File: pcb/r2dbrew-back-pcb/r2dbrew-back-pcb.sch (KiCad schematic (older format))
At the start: 38 parts, among them IC1 74HC238, IC2 TLC5971, IC3 FT230X, IC4 LM1117, IC5 ATMEGA328P, J1 USB, J2 PSI1, J3 PSI2, J4 RGB1, J5 RGB2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

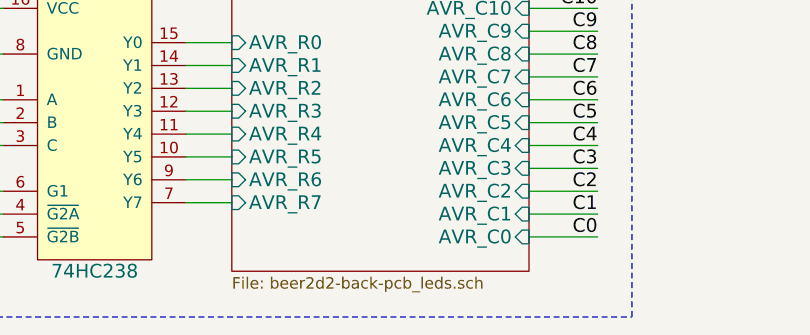
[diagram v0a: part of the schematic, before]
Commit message: cleanup after project rename
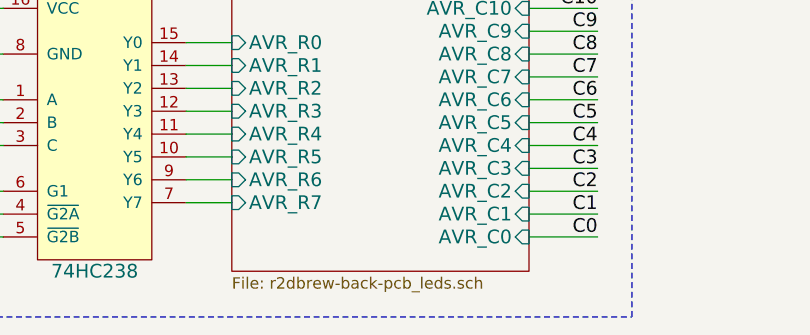
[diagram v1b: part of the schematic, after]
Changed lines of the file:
@@
 LIBS:ti-ic
 LIBS:uln-ic
-LIBS:beer2d2-back-pcb-cache
+LIBS:r2dbrew-back-pcb-cache
 EELAYER 24 0
 EELAYER END
@@
 encoding utf-8
 Sheet 1 2
-Title "beer2d2 (working title) back led panel and psi control"
-Date "27 jan 2014"
+Title "r2dbrew rear head led panel and psi control"
+Date "01 Apr 2014"
 Rev "0.1"
 Comp "Wiley Cousins, LLC. for Barton Gilley"
-Comment1 "shared under the terms of the Creative Commons Attribution Share-Alike 3.0 license"
+Comment1 "shared under the terms of the Creative Commons Attribution Share-Alike 4.0 license"
 Comment2 "open source hardware"
-Comment3 "github.com/mcous/beer2d2"
+Comment3 "github.com/mcous/r2dbrew"
 Comment4 ""
 $EndDescr
@@
 U 52E2D889
 F0 "LED Matrix" 50
-F1 "beer2d2-back-pcb_leds.sch" 50
+F1 "r2dbrew-back-pcb_leds.sch" 50
 F2 "AVR_R0" I L 2600 6400 60
 F3 "AVR_R1" I L 2600 6500 60
